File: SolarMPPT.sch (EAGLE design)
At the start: 47 parts, among them J1 CORTEX_DEBUG_SMD, J2 1X2-3.5MM, J3 1X2-3.5MM, J4 1X2-3.5MM, J5 1X2-3.5MM, J6 1X2-3.5MM, U1 STM32F091CCT6, U3 LTC1155, U6 3.3V, U7 LM22674MRX-5.0

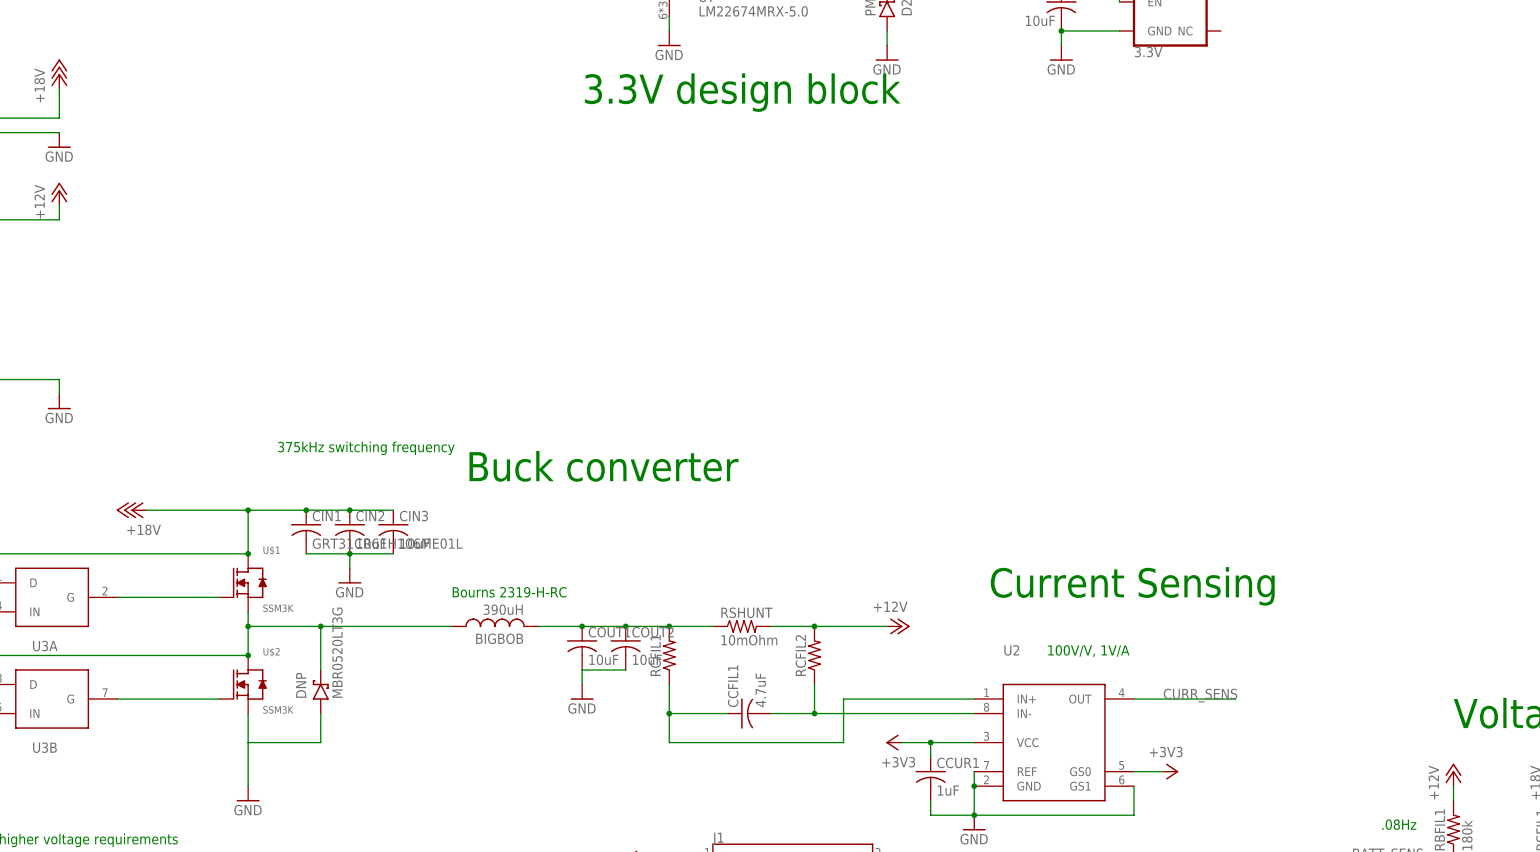
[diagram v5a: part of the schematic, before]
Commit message: added teensy, removed SD
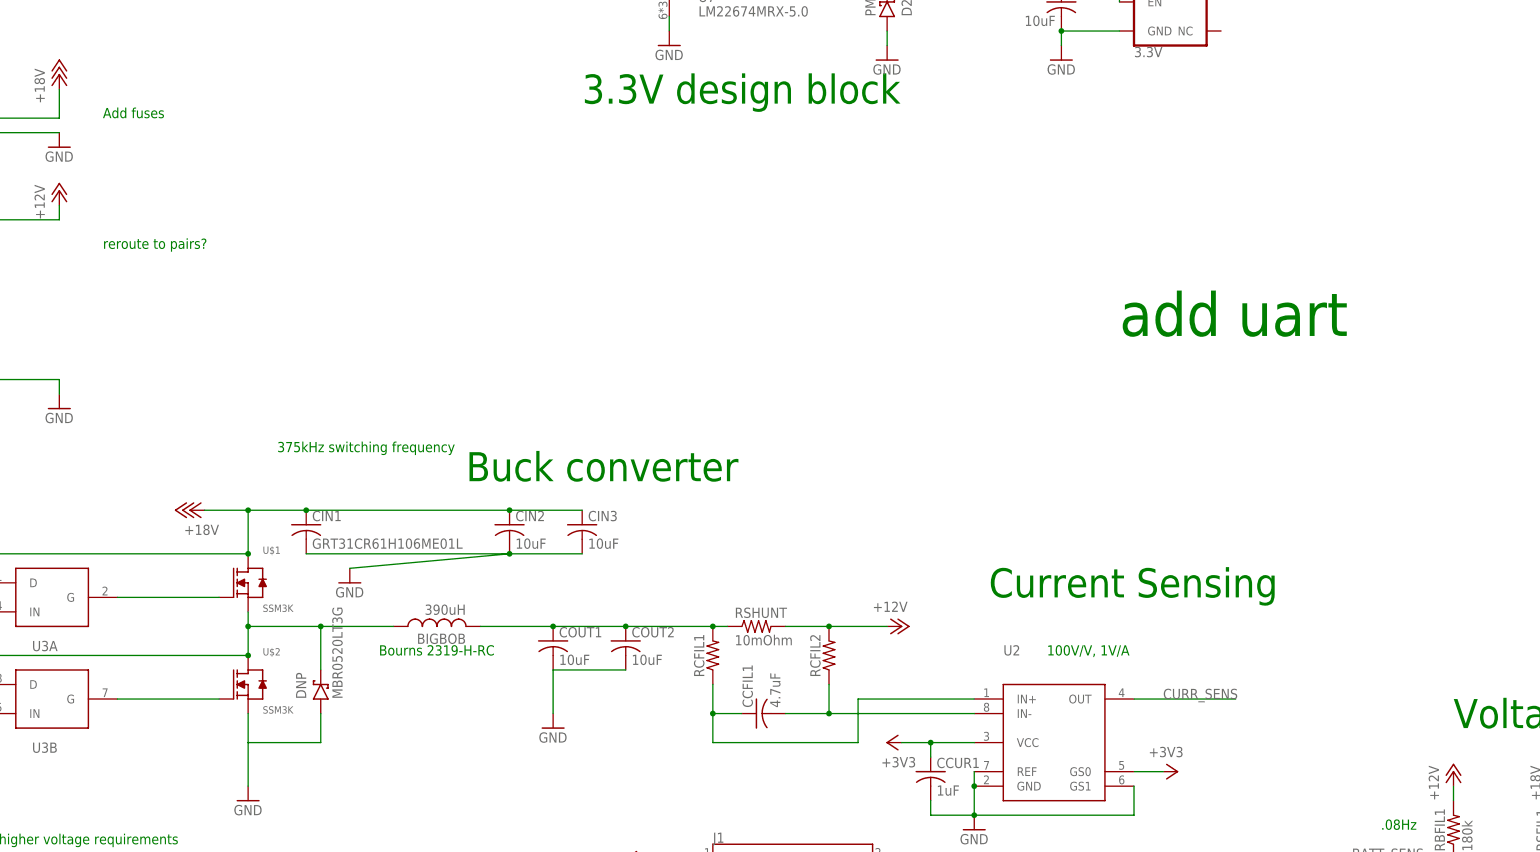
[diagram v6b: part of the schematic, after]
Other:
- note added: "Add fuses"
- note added: "add uart"
- note added: "reroute to pairs?"
- moved on the sheet: BIGBOB, CCFIL1, CIN2, CIN3, COUT1, RCFIL1, RCFIL2, RSHUNT

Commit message: removed 3.3v regulator (using teensy onboard)
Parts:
- removed CSD: 1uF, rcl:C-USC0805
- removed H1: MOLEX-502744, FormE:MOLEX-502744
- removed J1: CORTEX_DEBUG_SMD, SparkFun-Connectors:CORTEX_DEBUG_SMD
- removed U1: STM32F091CCT6, Microcontroller:STM32F091CCT6
- removed U6: 3.3V, SparkFun-IC-Power:V_REG_AP2112K-3.3V
- added U$3: TEENSY_3.1+4, FormE:TEENSY_3.1+4
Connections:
- removed net !RESET: J1.!RESET, U1.NRST
- removed net CS0: H1.CS, U1.PA4
- removed net MISO: H1.MISO, U1.PA6
- removed net MOSI: H1.MOSI, U1.PA7
- removed net N$1: J1.SWDCLK/TCK, U1.PA14
- removed net N$2: J1.SWDIO/TMS, U1.PA13
- removed net SCLK: H1.SCLK, U1.PA5
- net +3V3: no longer CSD.1, H1.VDD, J1.VCC, U1.VBAT, U1.VDD, U1.VDD1, U1.VDDA, U1.VDDIO2, U6.OUT
- net +5V: no longer U6.EN, U6.IN
- net BATT_SENS: no longer U1.PA1
- net CURR_SENS: no longer U1.PA0
- net GND: no longer CSD.2, H1.SHIELD, H1.VSS, J1.GND@3, J1.GND@5, J1.GNDDTCT, U1.VSS, U1.VSS1, U1.VSS2, U1.VSSA, U6.GND
- net SOLAR_SENS: no longer U1.PA2
- net TIME_OUT: no longer U1.PA8
- net TIME_OUTN: no longer U1.PB13
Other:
- note removed: "SD card"

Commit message: routed!
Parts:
- removed CVDD1, CVDDIO2B: 100nF, rcl:C-USC0805
- removed CVDD2, CVDDIO2A: 4.7uF, rcl:C-USC0805
- removed CVDDA1: 1uF, rcl:C-USC0805
- removed CVDDA2: 10nF, rcl:C-USC0805
- removed J4, J5: 1X2-3.5MM, adafruit:1X2-3.5MM
- added JP1: (no value), pinhead:PINHD-1X13
- U$3: value TEENSY_3.1+4 -> TEENSY_3.1_BASIC; device FormE:TEENSY_3.1+4 -> FormE:TEENSY_3.1_BASIC
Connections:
- new net 3V3B: JP1.2
- new net BUSY: JP1.12, U$3.9/RX2/PWM
- new net D/C: JP1.8, U$3.5/PWM
- new net ECS: JP1.7, U$3.4/CAN-RX-PWM
- new net ENA: JP1.13, U$3.10/TX2/PWM
- new net MISO: JP1.5, U$3.12/MISO
- new net MOSI: JP1.6, U$3.11/MOSI
- new net RST: JP1.11, U$3.8/TX3
- new net SCLK: JP1.4, U$3.13/SCK/LED
- new net SDCS: JP1.10, U$3.7/RX3
- new net SRCS: JP1.9, U$3.6/PWM
- net +12V: no longer J2.1, J3.1
- net +18V: now also J6.2; no longer J6.1
- net +3V3: now also U$3.3.3V; no longer CVDD1.1, CVDD2.1, CVDDA1.1, CVDDA2.1, CVDDIO2A.1, CVDDIO2B.1
- net +5V: now also JP1.1, U$3.VIN
- net BATT_SENS: now also U$3.15/A1/T
- net CURR_SENS: now also U$3.16/A2/T
- net GND: now also J2.1, J3.1, J6.1, JP1.3, U$3.AGND, U$3.GND; no longer CVDD1.2, CVDD2.2, CVDDA1.2, CVDDA2.2, CVDDIO2A.2, CVDDIO2B.2, J4.1, J4.2, J5.1, J5.2, J6.2
- net SOLAR_SENS: now also U$3.14/A0
- net TIME_OUT: now also U$3.23/A9/T/PWM
- net TIME_OUTN: now also U$3.22/A8/T/PWM
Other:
- note added: "EPD breakout"
- note removed: "VDDA"
- note removed: "VDDIO2"
- note removed: "ferrite?"
